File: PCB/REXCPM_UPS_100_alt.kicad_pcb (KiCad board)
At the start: 2 copper layers, 51.3 x 18.3 mm, 11 parts, among them J1 Model_100_System_BUS, J2 SM04B, U1 742G02

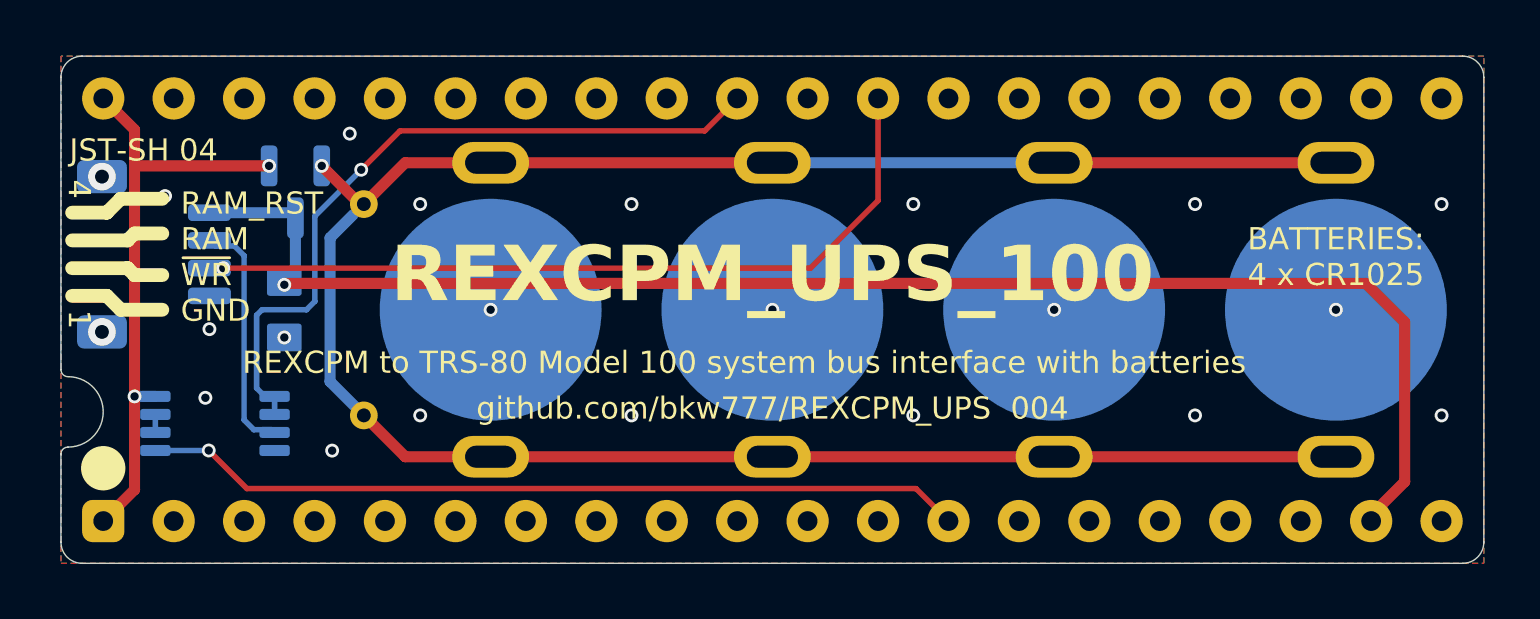
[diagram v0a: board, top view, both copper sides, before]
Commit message: 4-cells, add gnd wire, jst-sh connector
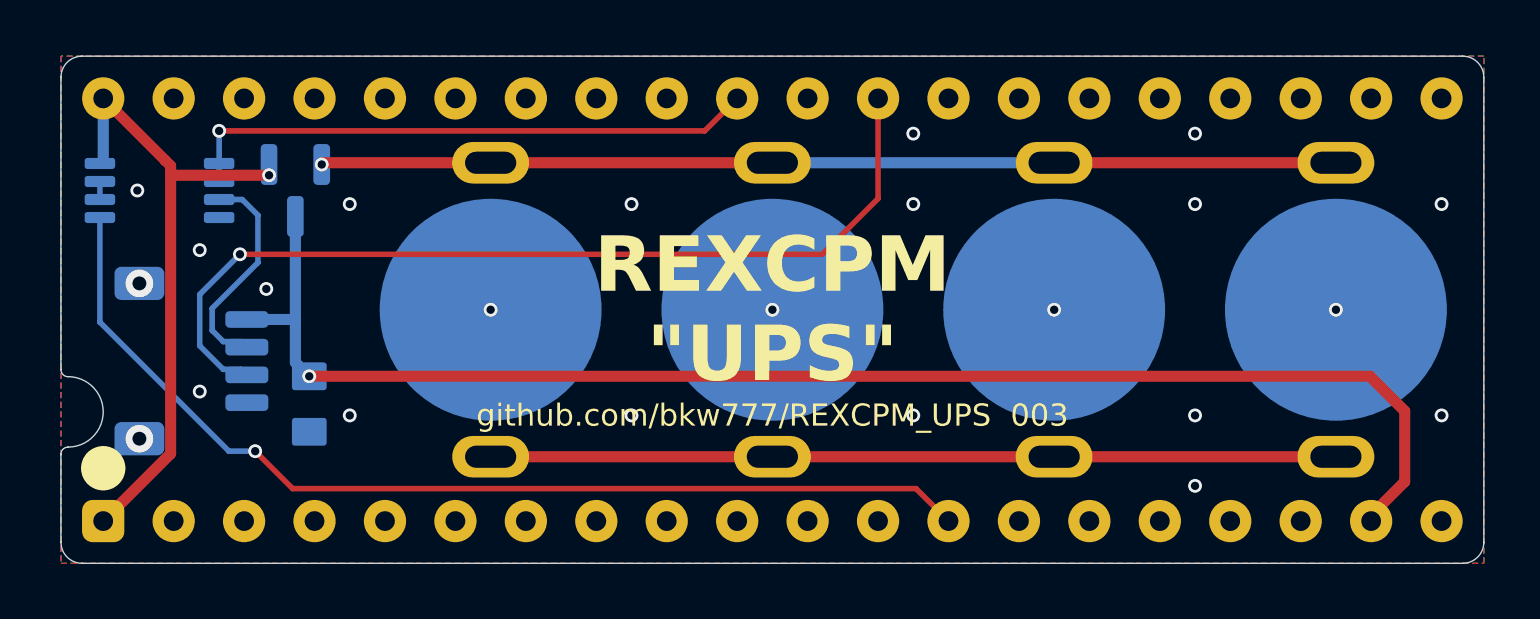
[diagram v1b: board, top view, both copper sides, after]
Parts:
- removed REF** (x2): TestPoint_THTPad_D1.0mm_Drill0.5mm, 000_LOCAL:TestPoint_THTPad_D1.0mm_Drill0.5mm
- J2: value SM04B -> Conn_01x04_Pin
- moved U1 8.63 mm to (114.4, 100.5)
- moved J2 4.08 mm to (115.6, 106.6)
- moved C1 3.52 mm to (119.8, 108.2)
- moved D1 0.05 mm to (119.3, 100.5)
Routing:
- net /BATT+: track 81.6 -> 67.1 mm
- net /IO/~{M}: track 29.7 -> 37.3 mm
- net /A15: track 26.4 -> 21.0 mm
- net /~{WR}: track 28.8 -> 33.5 mm
- net /RAM_RST: track 54.3 -> 52.2 mm
- net VBUS: track 21.8 -> 23.6 mm, vias 2 -> 1
- net /RAM: track 8.69 -> 7.97 mm
- net GND: vias 22 -> 23
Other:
- board text added: "REXCPM {dblquote}UPS{dblquote}"
- board text removed: "${TITLE}"
- board text removed: "1"
- board text removed: "3031"
- board text removed: "4"
- board text removed: "BATTERIES: 4 x CR1025"
- board text removed: "CR1025"
- board text removed: "JST-SH 04"
- board text removed: "Keystone"
- board text removed: "RAM_RST RAM ~{WR} GND"
- board text removed: "REXCPM to TRS-80 Model 100 system bus interface with batteries"
